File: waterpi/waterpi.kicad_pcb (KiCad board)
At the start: 2 copper layers, 65 x 56 mm, 38 parts, among them J1 RPi, J10 OUT6, J11 OUT7, J14 ADC0, J15 ADC1, J16 ADC2, J17 ADC3, J18 ADC4, J19 ADC5, J2 Conn_01x10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

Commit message: Remove old schematic
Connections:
- U1 pad 15: +3.3V -> +5V
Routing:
- net +3.3V: track 85.5 -> 72.9 mm
- net +5V: track 140.7 -> 150.5 mm
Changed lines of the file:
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@@
 			(layers "F.Cu" "F.Paste" "F.Mask")
 			(roundrect_rratio 0.25)
-			(net 42 "+3.3V")
+			(net 22 "+5V")
 			(pinfunction "Vref")
 			(pintype "power_in")
@@
 	)
 	(segment
+		(start 133.35 93.98)
+		(end 134.525 95.155)
+		(width 0.25)
+		(layer "F.Cu")
+		(net 1)
+	)
+	(segment
 		(start 129.6 136.25)
 		(end 129.789 136.061)
@@
 	)
 	(segment
+		(start 137.255 95.155)
+		(end 138.43 93.98)
+		(width 0.25)
+		(layer "F.Cu")
+		(net 1)
+	)
+	(segment
 		(start 100.563 136.25)
 		(end 100.704 136.109)
@@
 	)
 	(segment
+		(start 134.525 95.155)
+		(end 137.255 95.155)
+		(width 0.25)
+		(layer "F.Cu")
+		(net 1)
+	)
+	(segment
 		(start 136.25 136.25)
 		(end 137.055 136.25)
@@
 	)
 	(segment
-		(start 134.525001 92.804999)
-		(end 137.254999 92.804999)
-		(width 0.25)
-		(layer "B.Cu")
-		(net 1)
-	)
-	(segment
 		(start 136.2 136.3)
 		(end 128.8 136.3)
@@
 	)
 	(segment
-		(start 137.254999 92.804999)
-		(end 137.580001 93.130001)
-		(width 0.25)
-		(layer "B.Cu")
-		(net 1)
-	)
-	(segment
 		(start 107.100001 92.289999)
 		(end 107.95 91.44)
@@
 	)
 	(segment
-		(start 133.35 93.98)
-		(end 134.525001 92.804999)
-		(width 0.25)
-		(layer "B.Cu")
-		(net 1)
-	)
-	(segment
 		(start 104.234999 92.615001)
 		(end 106.774999 92.615001)
@@
 	)
 	(segment
-		(start 137.580001 93.130001)
-		(end 138.43 93.98)
-		(width 0.25)
-		(layer "B.Cu")
-		(net 1)
-	)
-	(segment
 		(start 99.75 136.25)
 		(end 99.7 136.3)
@@
 	)
 	(segment
+		(start 134.18 102.47)
+		(end 126.97 102.47)
+		(width 0.25)
+		(layer "F.Cu")
+		(net 22)
+	)
+	(segment
 		(start 96 95.77)
 		(end 97.79 93.98)
@@
 	)
 	(segment
+		(start 126.97 102.47)
+		(end 125.75 101.25)
+		(width 0.25)
+		(layer "F.Cu")
+		(net 22)
+	)
+	(segment
 		(start 97.79 93.98)
 		(end 99 92.77)
@@
 	)
 	(segment
+		(start 134.825 101.825)
+		(end 134.18 102.47)
+		(width 0.25)
+		(layer "F.Cu")
+		(net 22)
+	)
+	(segment
 		(start 99 92.65)
 		(end 99 90.5)
@@
 	)
 	(segment
-		(start 128 101.700908)
-		(end 128.769092 102.47)
-		(width 0.25)
-		(layer "F.Cu")
-		(net 42)
-	)
-	(segment
 		(start 118.11 91.44)
 		(end 120.05 89.5)
@@
 	)
 	(segment
-		(start 134.525 90.525)
-		(end 134.525 94.466701)
-		(width 0.25)
-		(layer "F.Cu")
-		(net 42)
-	)
-	(segment
-		(start 128 100.679092)
-		(end 128 101.700908)
-		(width 0.25)
-		(layer "F.Cu")
-		(net 42)
-	)
-	(segment
-		(start 134.5 90.5)
-		(end 134.525 90.525)
-		(width 0.25)
-		(layer "F.Cu")
-		(net 42)
-	)
-	(segment
-		(start 128.769092 102.47)
-		(end 134.18 102.47)
-		(width 0.25)
-		(layer "F.Cu")
-		(net 42)
-	)
-	(segment
-		(start 134.525 94.466701)
-		(end 129.491701 99.5)
+		(start 134.75 100.48)
+		(end 134.825 100.555)
 		(width 0.25)
 		(layer "F.Cu")
@@
 	)
 	(segment
-		(start 134.825 101.825)
-		(end 134.825 100.555)
+		(start 134.75 99.5)
+		(end 134.75 100.48)
 		(width 0.25)
 		(layer "F.Cu")
@@
 		(net 42)
 	)
-	(segment
-		(start 129.491701 99.5)
-		(end 129.179092 99.5)
-		(width 0.25)
-		(layer "F.Cu")
-		(net 42)
-	)
-	(segment
-		(start 134.18 102.47)
-		(end 134.825 101.825)
-		(width 0.25)
-		(layer "F.Cu")
-		(net 42)
-	)
-	(segment
-		(start 129.179092 99.5)
-		(end 128 100.679092)
-		(width 0.25)
-		(layer "F.Cu")
-		(net 42)
-	)
 	(via
 		(at 129.625584 90.249999)
@@
 	)
 	(via
-		(at 134.5 90.5)
+		(at 134.75 99.5)
 		(size 0.6)
 		(drill 0.4)
@@
 	)
 	(segment
+		(start 134.525 99.275)
+		(end 134.75 99.5)
+		(width 0.25)
+		(layer "B.Cu")
+		(net 42)
+	)
+	(segment
+		(start 134.525 90.525)
+		(end 134.525 99.275)
+		(width 0.25)
+		(layer "B.Cu")
+		(net 42)
+	)
+	(segment
 		(start 115.0375 101.22)
 		(end 112.3775 103.88)
@@
 		(width 0.25)
 		(layer "B.Cu")
+		(net 42)
+	)
+	(segment
+		(start 134.5 90.5)
+		(end 134.525 90.525)
+		(width 0.25)
+		(layer "B.Cu")

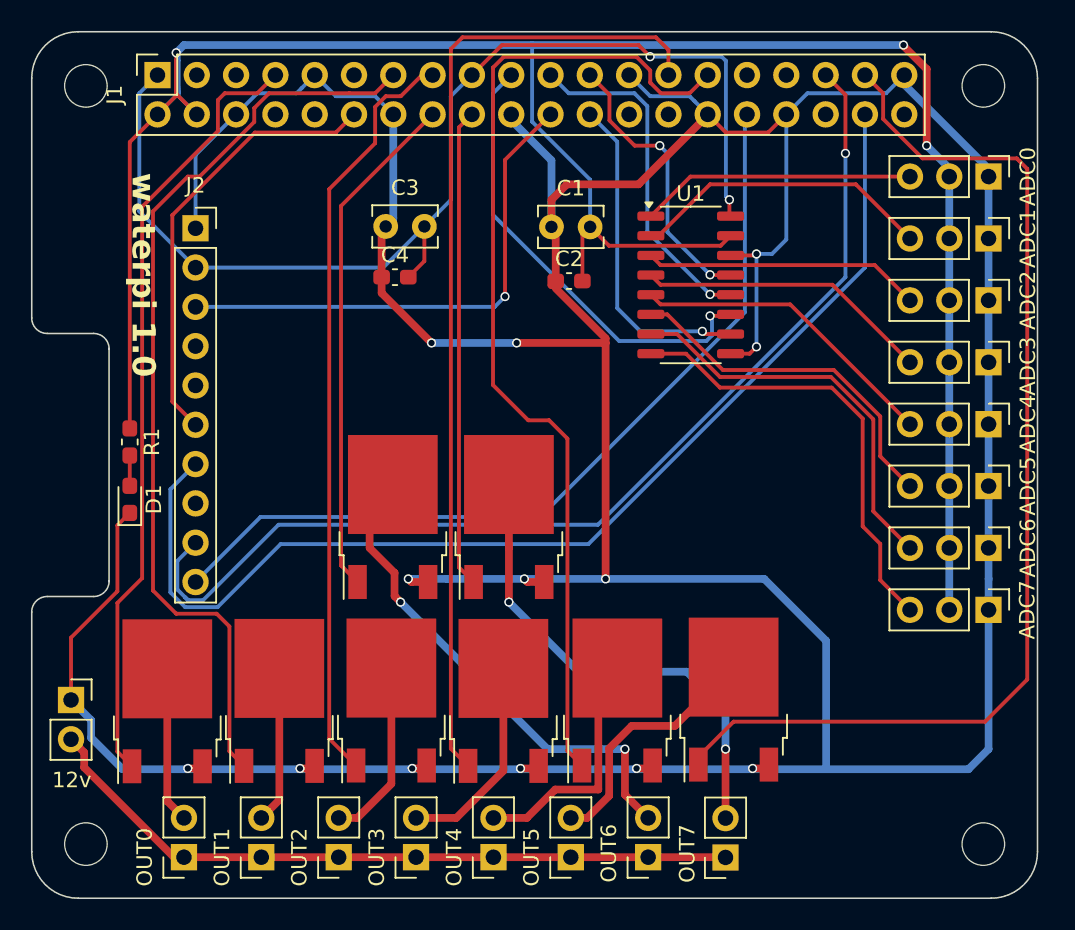
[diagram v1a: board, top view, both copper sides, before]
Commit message: Use SOT-223
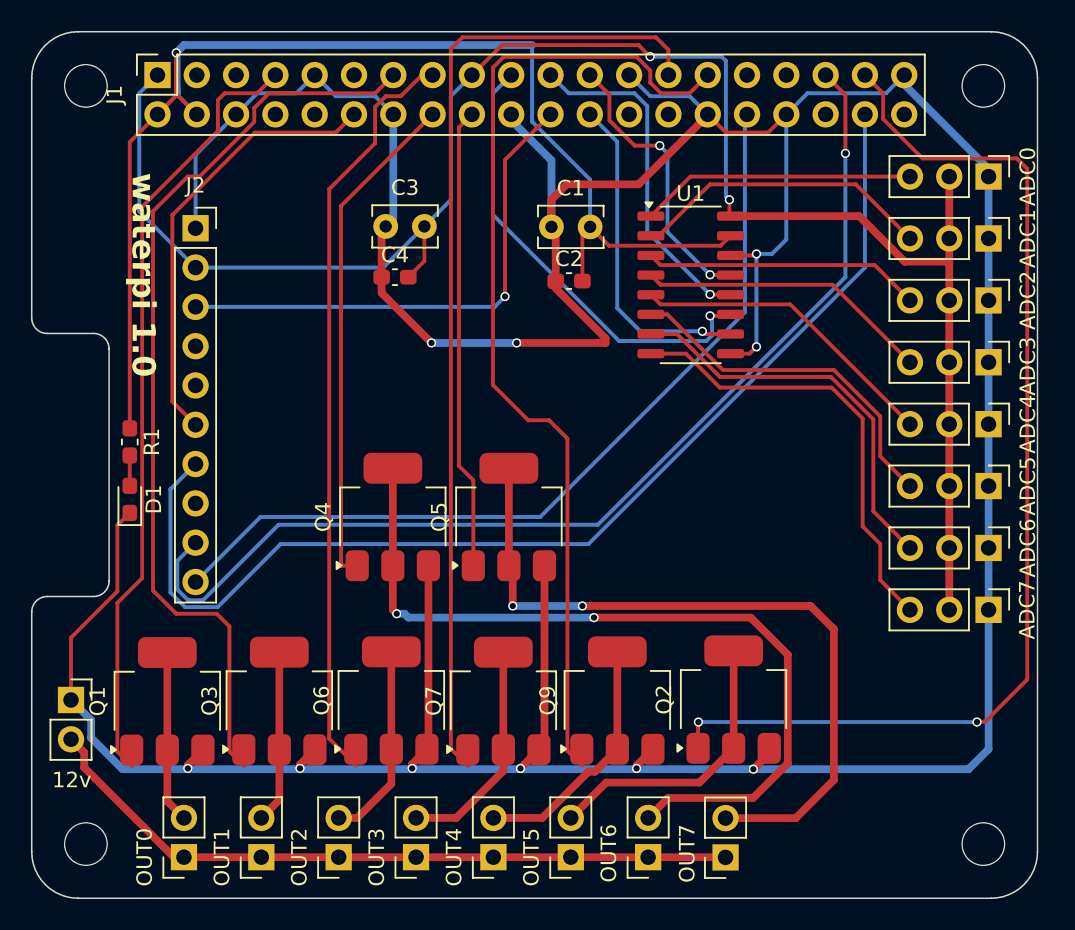
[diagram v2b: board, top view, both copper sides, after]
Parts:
- Q1, Q2, Q3, Q4, Q5, Q6, Q7, Q9: footprint Package_TO_SOT_SMD:TO-252-2 -> Package_TO_SOT_SMD:SOT-223-3_TabPin2
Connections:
- J14 pad 2: +5V -> +3.3V
- J15 pad 2: +5V -> +3.3V
- J16 pad 2: +5V -> +3.3V
- J17 pad 2: +5V -> +3.3V
- J18 pad 2: +5V -> +3.3V
- J19 pad 2: +5V -> +3.3V
- J20 pad 2: +5V -> +3.3V
- J21 pad 2: +5V -> +3.3V
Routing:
- net +5V: track 150.5 -> 88.8 mm, vias 3 -> 1
- net +3.3V: track 72.9 -> 116.1 mm
- net GND: track 305.8 -> 275.3 mm, vias 13 -> 10
- net /OUT6: track 32.6 -> 53.4 mm
- net /OUT7: track 31.5 -> 48.1 mm
- net /OUT5: track 16.4 -> 18.7 mm
- net /GPIO24: track 31.0 -> 29.9 mm
- net /GPIO22: track 49.1 -> 48.4 mm
- net /GPIO26: track 70.8 -> 71.3 mm, vias 0 -> 2
- net /CH1: track 19.6 -> 19.1 mm
